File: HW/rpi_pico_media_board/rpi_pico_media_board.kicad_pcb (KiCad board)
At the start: 2 copper layers, 134 parts, among them IC100 LS1205EVD33, J200 Conn_01x04_Pin, J201 Conn_01x04_Pin, J300 AudioJack3_Ground_SwitchTR, J400 TF-01A, Q100 T2N7002AK, Q500 T2N7002AK, Q501 T2N7002AK, Q502 T2N7002AK, SW200 SW_DPDT_XLX, U100 HT7533-1, U200 RaspberryPi_Pico, U202 mems-mic, U203 mems-mic, U300 PCM5102A, U600 PCF8563TS, Y600 32768Hz

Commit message: DRC cleanup
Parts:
- removed C109, C110: 22uF, Capacitor_SMD:C_0603_1608Metric
- removed IC100: LS1205EVD33, rpi_pico_media_board_power:LS1205EVD33
- removed J100: ~, Connector_BarrelJack:BarrelJack_GCT_DCJ200-10-A_Horizontal
- removed R108: 10R, Resistor_SMD:R_0805_2012Metric
- removed R109: 510R, Resistor_SMD:R_0402_1005Metric
- removed R110: 12kR, Resistor_SMD:R_0402_1005Metric
- removed SW500, SW501, SW502, SW503, SW504, SW505, SW506, SW507, SW508, SW509, SW510, SW511: ~, rpi_pico_media_board:SW_PUSH_6mm_H5mm
- added J1: Barrel_Jack_Switch_Pin3Ring, Connector_BarrelJack:BarrelJack_GCT_DCJ200-10-A_Horizontal, F.Cu at (205.8, 18.3)
- added L101: 2u2H, Inductor_SMD:L_1008_2520Metric, F.Cu at (186.2, 125.8)
- added R306: 22R, Resistor_SMD:R_0603_1608Metric, F.Cu at (206.7, 36.2)
- added R307: 22R, Resistor_SMD:R_0603_1608Metric, F.Cu at (206.7, 38.8)
- added R308: 470R, Resistor_SMD:R_0805_2012Metric, F.Cu at (202.5, 36.5)
- added R309: 470R, Resistor_SMD:R_0805_2012Metric, F.Cu at (202.5, 39.4)
- added U500: SW, rpi_pico_media_board:SW_PUSH_6mm_H5mm, F.Cu at (189.7, 18.3)
- added U501: SW, rpi_pico_media_board:SW_PUSH_6mm_H5mm, F.Cu at (189.7, 26.8)
- added U502: SW, rpi_pico_media_board:SW_PUSH_6mm_H5mm, F.Cu at (189.7, 35.4)
- added U503: SW, rpi_pico_media_board:SW_PUSH_6mm_H5mm, F.Cu at (189.7, 43.9)
- added U504: SW, rpi_pico_media_board:SW_PUSH_6mm_H5mm, F.Cu at (222.9, 17.4)
- added U505: SW, rpi_pico_media_board:SW_PUSH_6mm_H5mm, F.Cu at (222.9, 25.9)
- added U506: SW, rpi_pico_media_board:SW_PUSH_6mm_H5mm, F.Cu at (222.9, 34.5)
- added U507: SW, rpi_pico_media_board:SW_PUSH_6mm_H5mm, F.Cu at (222.9, 43.0)
- added U508: SW, rpi_pico_media_board:SW_PUSH_6mm_H5mm, F.Cu at (222.9, 51.6)
- added U509: SW, rpi_pico_media_board:SW_PUSH_6mm_H5mm, F.Cu at (233.5, 17.4)
- added U510: SW, rpi_pico_media_board:SW_PUSH_6mm_H5mm, F.Cu at (233.5, 25.9)
- added U511: SW, rpi_pico_media_board:SW_PUSH_6mm_H5mm, F.Cu at (233.5, 34.5)
- C100: value 22uF -> 1uF; footprint Capacitor_SMD:C_1206_3216Metric -> Capacitor_SMD:C_0603_1608Metric
- C101: value 100nF -> 1uF; footprint Capacitor_SMD:C_0402_1005Metric -> Capacitor_SMD:C_0603_1608Metric
- C102: value 100nF -> 22uF; footprint Capacitor_SMD:C_0402_1005Metric -> Capacitor_SMD:C_1206_3216Metric
- C103: value 22uF -> 4u7F; footprint Capacitor_SMD:C_1206_3216Metric -> Capacitor_SMD:C_0603_1608Metric
- C104: value 22uF -> 22pF; footprint Capacitor_SMD:C_1206_3216Metric -> Capacitor_SMD:C_0603_1608Metric
- C105: value 4u7F -> 22uF; footprint Capacitor_SMD:C_0603_1608Metric -> Capacitor_SMD:C_1206_3216Metric
- C106: value 22pF -> 22uF; footprint Capacitor_SMD:C_0402_1005Metric -> Capacitor_SMD:C_1206_3216Metric
- L100: value 2u2H -> 10nH; footprint Inductor_SMD:L_1008_2520Metric -> Inductor_SMD:L_0603_1608Metric
- R100, R107: value 100kR -> 12kR; footprint Resistor_SMD:R_0402_1005Metric -> Resistor_SMD:R_0603_1608Metric
- R101: value 4k7R -> 12kR; footprint Resistor_SMD:R_0402_1005Metric -> Resistor_SMD:R_0603_1608Metric
- R102, R104: value 12kR -> 100kR; footprint Resistor_SMD:R_0402_1005Metric -> Resistor_SMD:R_0603_1608Metric
- R103: value 12kR -> 453kR; footprint Resistor_SMD:R_0402_1005Metric -> Resistor_SMD:R_0603_1608Metric
- R105: value 100kR -> 10R; footprint Resistor_SMD:R_0402_1005Metric -> Resistor_SMD:R_0805_2012Metric
- R106: value 453kR -> 510R; footprint Resistor_SMD:R_0402_1005Metric -> Resistor_SMD:R_0603_1608Metric
- R304, R305: value 470R -> 22R; footprint Resistor_SMD:R_0805_2012Metric -> Resistor_SMD:R_0603_1608Metric
- R507, R508, R509, R510, R511, R512: footprint Resistor_SMD:R_0402_1005Metric -> Resistor_SMD:R_0603_1608Metric
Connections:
- C101 pad 1: /[1]Power/PWR_EN -> +5V
- C102 pad 1: /[1]Power/EFUSE_SS -> +5V
- C103 pad 1: +5V -> PG_3V3
- C104 pad 1: +5V -> +3.3V
- C104 pad 2: GND -> /[1]Power/FB_3V3
- C105 pad 1: PG_3V3 -> +3.3V
- C106 pad 2: /[1]Power/FB_3V3 -> GND
- C107 pad 1: +3.3V -> /[1]Power/+5V_FILT
- C108 pad 1: +3.3V -> +3.3VA
- J400 pad 6: unconnected-(J400-VSS-Pad6) -> GND
- L100 pad 1: /[1]Power/SW_3V3 -> VCC
- L100 pad 2: +3.3V -> +5V
- R100 pad 1: VCC -> PG_3V3
- R100 pad 2: /[1]Power/PWR_EN -> +5V
- R101 pad 1: /[1]Power/EFUSE_ILIM -> +5V
- R101 pad 2: GND -> /[1]Power/EN_3V3
- R102 pad 1: /[1]Power/EFUSE_VCP -> PG_3V3
- R102 pad 2: VCC -> GND
- R103 pad 1: PG_3V3 -> +3.3V
- R103 pad 2: +5V -> /[1]Power/FB_3V3
- R104 pad 1: +5V -> /[1]Power/FB_3V3
- R104 pad 2: /[1]Power/EN_3V3 -> GND
- R105 pad 1: PG_3V3 -> /[1]Power/+5V_FILT
- R105 pad 2: GND -> +5V
- R106 pad 1: +3.3V -> /[1]Power/LED_PWR_A
- R106 pad 2: /[1]Power/FB_3V3 -> +5V
- R107 pad 1: /[1]Power/FB_3V3 -> Net-(Q100-G)
- R107 pad 2: GND -> PG_3V3
- R304 pad 1: /[3]PCM5102/OUTR -> GND
- R304 pad 2: /[3]PCM5102/OUT_R -> /[3]PCM5102/FLT
- R305 pad 1: /[3]PCM5102/OUTL -> GND
- R305 pad 2: /[3]PCM5102/OUT_L -> /[3]PCM5102/DEMP
- U300 pad 10: GND -> /[3]PCM5102/DEMP
- U300 pad 11: GND -> /[3]PCM5102/FLT
- U300 pad 16: GND -> /[3]PCM5102/FMT
- U300 pad 17: +3.3V -> /[3]PCM5102/XSMT
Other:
- copper layers 2 -> 4
- rule pad_to_mask_clearance: 0 -> 0.038

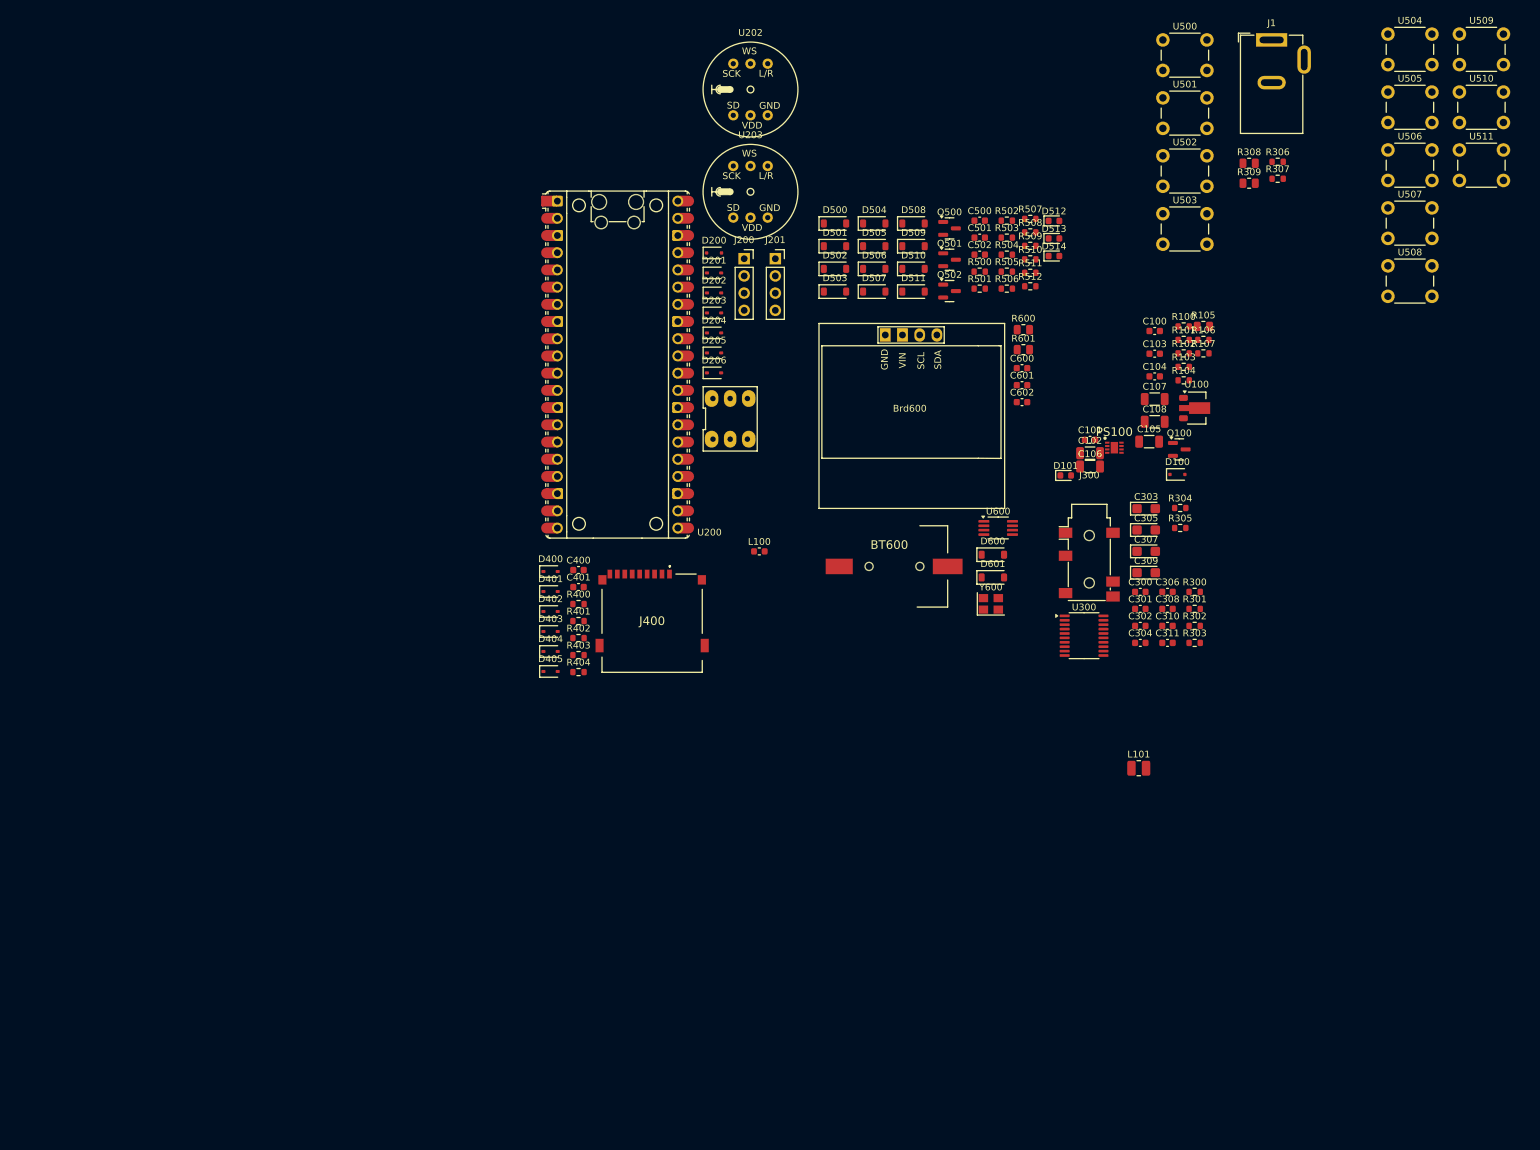
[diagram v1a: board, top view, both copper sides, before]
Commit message: PCB initial placement
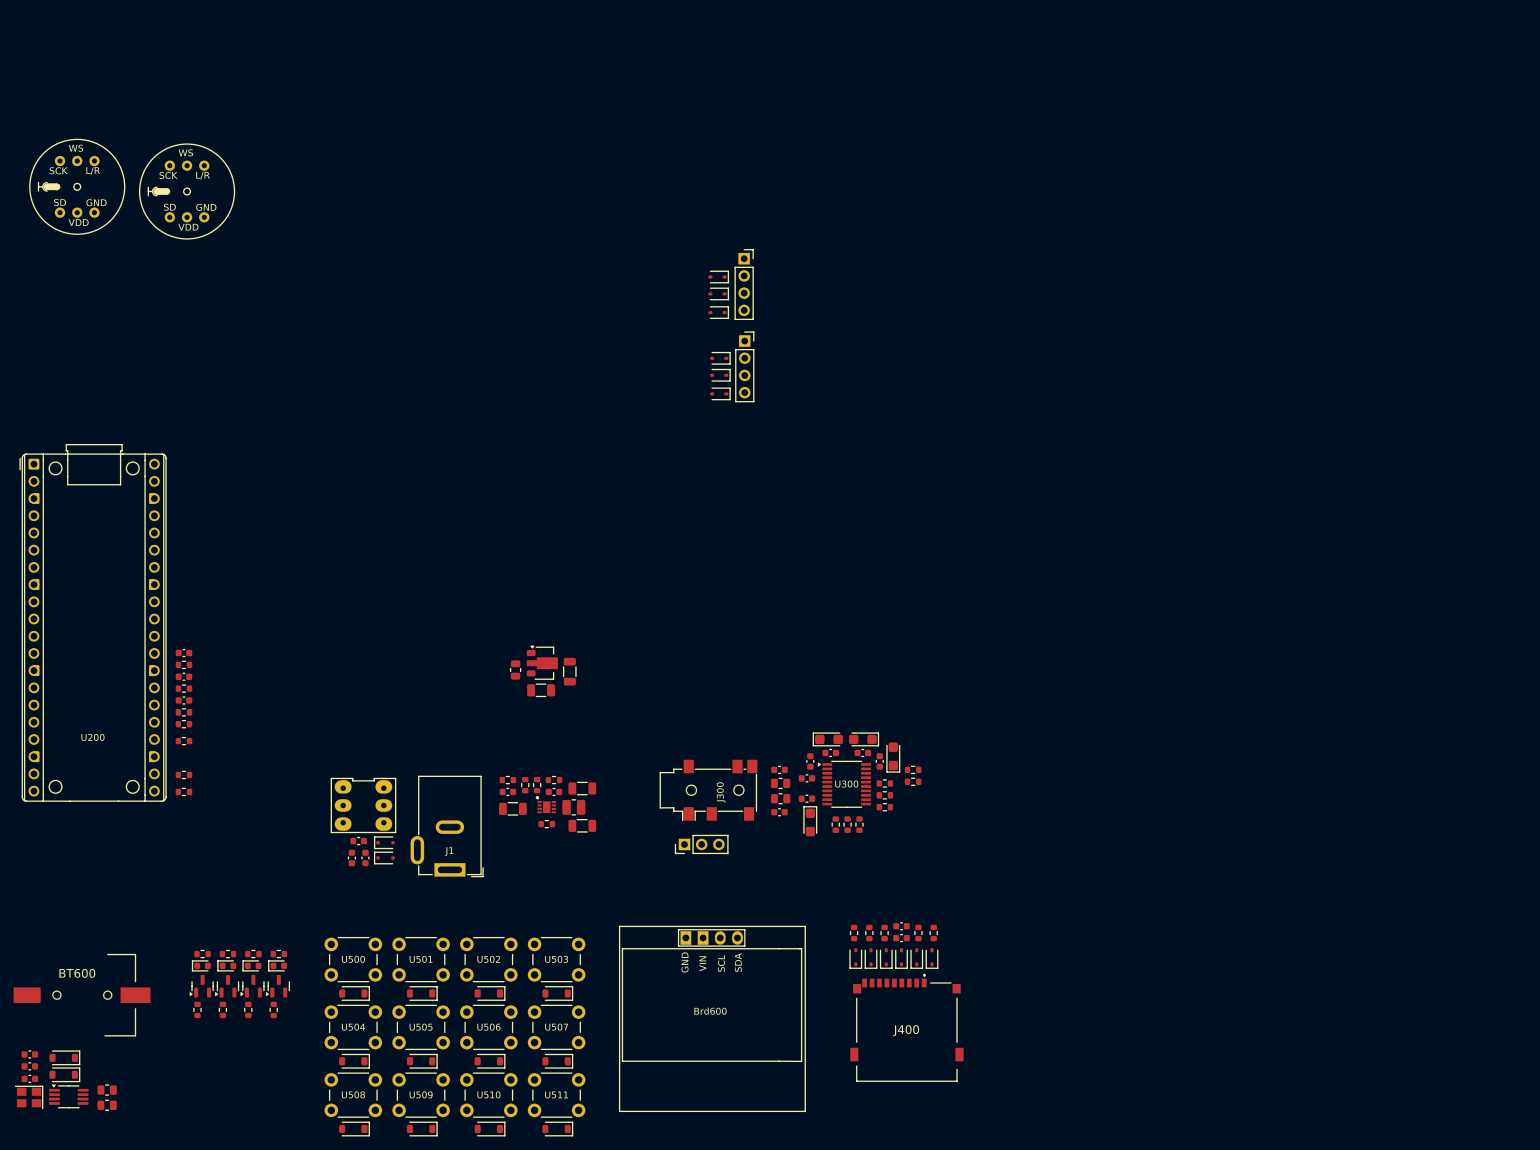
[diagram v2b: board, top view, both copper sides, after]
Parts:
- added J301: Conn_01x03_Pin, Connector_PinHeader_2.54mm:PinHeader_1x03_P2.54mm_Vertical, F.Cu at (119.1, 137.0)
- U200: footprint Module_RaspberryPi_Pico:RaspberryPi_Pico_Common -> Module_RaspberryPi_Pico:RaspberryPi_Pico_Common_THT
- moved U509 219.8 mm to (77.0, 171.8)
- moved U504 212.5 mm to (67.0, 161.8)
- moved U510 206.7 mm to (87.0, 171.8)
- moved U505 199.4 mm to (77.0, 161.8)
- moved U508 196.9 mm to (67.0, 171.8)
- moved U511 193.6 mm to (97.0, 171.8)
- moved U506 186.2 mm to (87.0, 161.8)
- moved U500 181.3 mm to (67.0, 151.8)
- moved C600 179.1 mm to (22.5, 169.8), turned to 180 degrees
- moved C602 177.3 mm to (22.5, 171.6), turned to 180 degrees
- moved R600 177.2 mm to (33.9, 175.5), turned to 180 degrees
- moved C601 176.7 mm to (22.5, 168.0), turned to 180 degrees
- moved R601 173.9 mm to (33.9, 173.2), turned to 180 degrees
- moved U507 173.1 mm to (97.0, 161.8)
- moved J1 172.4 mm to (84.5, 140.8), turned to 180 degrees
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
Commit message: Very initial PCB layout
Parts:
- removed D204: PESD3V3L1BA,115, Diode_SMD:D_SOD-323
- added C109: 22uF, Capacitor_SMD:C_1206_3216Metric, F.Cu at (174.8, 115.5)
- added C110: 22uF, Capacitor_SMD:C_1206_3216Metric, F.Cu at (178.8, 112.5)
- added R108: 12kR, Resistor_SMD:R_0603_1608Metric, F.Cu at (242.8, 89.0)
- added U101: HT7533-1, Package_TO_SOT_SMD:SOT-89-3, F.Cu at (178.5, 116.5)
- BT600: moved to B.Cu
- J201: value Conn_01x04_Pin -> Conn_01x03; footprint Connector_PinSocket_2.54mm:PinSocket_1x04_P2.54mm_Vertical -> Connector_PinSocket_2.54mm:PinSocket_1x03_P2.54mm_Vertical
- R106: value 510R -> 10R; footprint Resistor_SMD:R_0603_1608Metric -> Resistor_SMD:R_0805_2012Metric
- R107: value 12kR -> 510R
- moved C601 214.2 mm to (216.5, 77.3), turned to 0 degrees
- moved D600 213.3 mm to (221.5, 79.9), turned to 0 degrees
- moved C600 212.0 mm to (213.2, 77.2)
- moved D601 209.6 mm to (216.2, 79.9)
- moved C602 209.5 mm to (211.4, 81.0)
- moved U600 209.5 mm to (217.1, 83.7)
- moved Y600 209.5 mm to (211.3, 83.8)
- moved R600 209.3 mm to (222.4, 84.6)
- moved R601 209.3 mm to (222.4, 82.3)
- moved BT600 206.1 mm to (216.3, 71.0)
- moved D101 193.4 mm to (241.1, 89.0), turned to -90 degrees
- moved Q100 191.6 mm to (238.1, 89.0), turned to 0 degrees
- moved R107 190.9 mm to (235.1, 89.0)
- moved R511 188.7 mm to (232.9, 89.0), turned to 90 degrees
- moved D514 187.7 mm to (231.2, 88.9), turned to -90 degrees
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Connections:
- net /[1]Power/+5V_FILT renamed /[1]Power/+5V_FILT_1
- C108 pad 1: +3.3VA -> +3.3VA_PCM
- C304 pad 1: +3.3VA -> +3.3VA_PCM
- C305 pad 1: +3.3VA -> +3.3VA_PCM
- C306 pad 1: +3.3VA -> +3.3VA_PCM
- C307 pad 1: +3.3VA -> +3.3VA_PCM
- R106 pad 1: /[1]Power/LED_PWR_A -> /[1]Power/+5V_FILT_2
- R107 pad 1: Net-(Q100-G) -> /[1]Power/LED_PWR_A
- R107 pad 2: PG_3V3 -> +5V
- U100 pad 3: +3.3VA -> +3.3VA_PCM
- U202 pad 1: +3.3VA -> +3.3VA_INMP
- U202 pad 6: +3.3VA -> +3.3VA_INMP
- U203 pad 1: +3.3VA -> +3.3VA_INMP
- U300 pad 1: +3.3VA -> +3.3VA_PCM
- U300 pad 20: +3.3VA -> +3.3VA_PCM

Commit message: minor layout update
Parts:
- moved R106 124.8 mm to (60.0, 93.2)
- moved C109 124.8 mm to (52.0, 93.2)
- moved C110 124.8 mm to (56.0, 90.2)
- moved U101 124.8 mm to (55.8, 94.2)
- moved R306 122.1 mm to (54.5, 80.8), turned to 0 degrees
- moved R307 121.2 mm to (54.5, 82.5), turned to 0 degrees
- moved R302 116.1 mm to (57.0, 82.7), turned to 90 degrees
- moved R304 114.9 mm to (54.4, 79.0), turned to 0 degrees
- moved R301 114.5 mm to (58.8, 82.7), turned to 90 degrees
- moved R404 113.8 mm to (55.0, 101.7), turned to -90 degrees
- moved R303 113.2 mm to (54.4, 77.2), turned to 0 degrees
- moved R300 112.8 mm to (60.5, 82.7), turned to 90 degrees
- moved R305 111.5 mm to (54.4, 75.5), turned to 0 degrees
- moved R400 111.4 mm to (57.2, 101.5), turned to -90 degrees
- moved D405 110.6 mm to (55.2, 105.1), turned to 90 degrees
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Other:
- board outline added: 100 x 80 mm

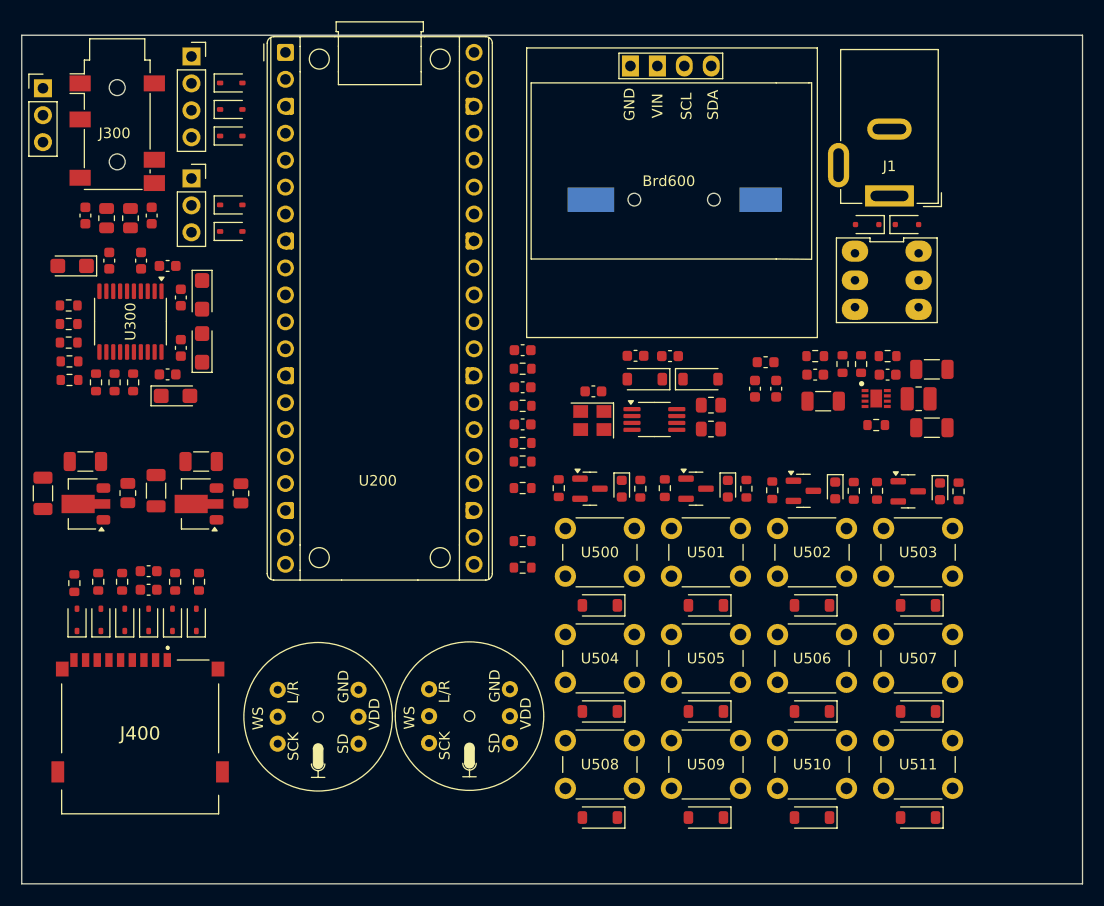
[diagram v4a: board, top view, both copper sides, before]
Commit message: PCB initial layout
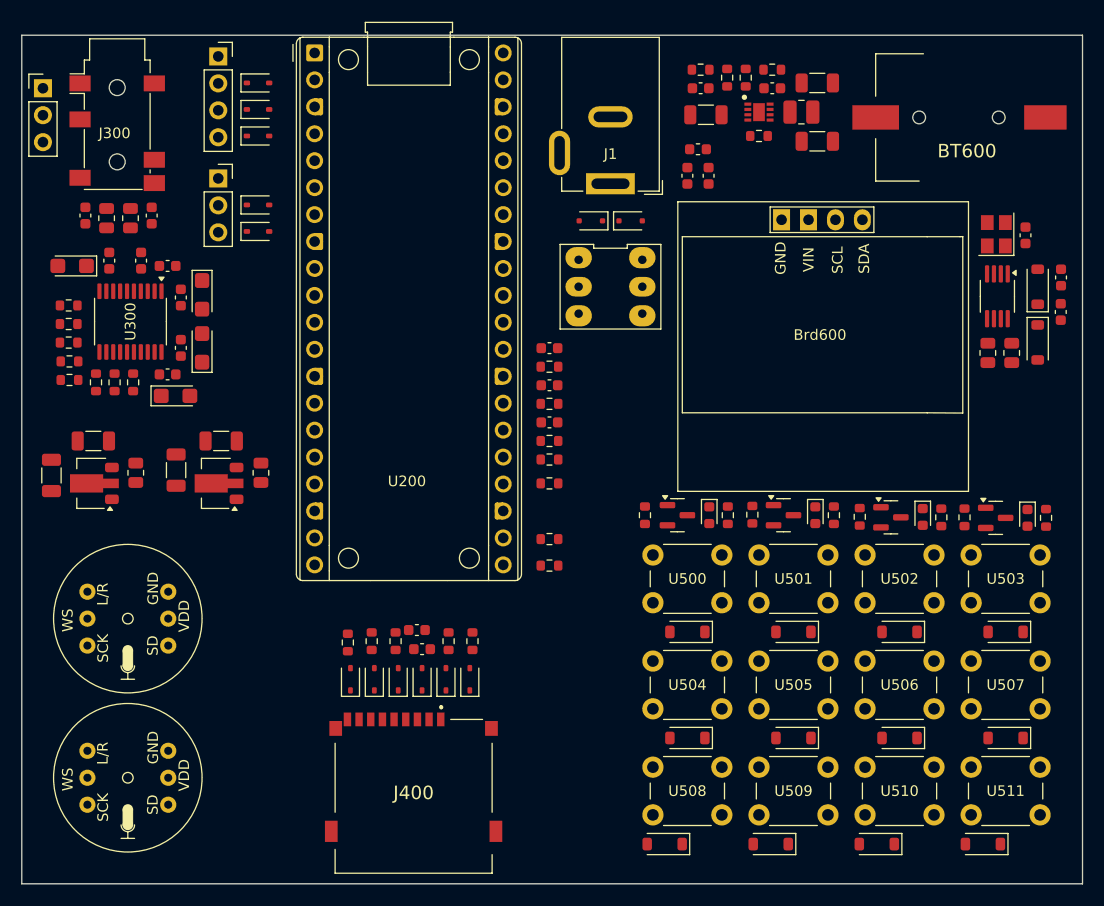
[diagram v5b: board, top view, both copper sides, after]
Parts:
- BT600: moved to F.Cu
- moved C602 43.3 mm to (144.6, 68.9), turned to 90 degrees
- moved Y600 41.9 mm to (141.9, 68.8), turned to 90 degrees
- moved C600 40.8 mm to (148.0, 72.8), turned to 90 degrees
- moved D601 38.0 mm to (145.8, 73.7), turned to 90 degrees
- moved C601 37.1 mm to (147.9, 76.1), turned to -90 degrees
- moved U600 34.4 mm to (142.0, 74.6), turned to -90 degrees
- moved U203 32.7 mm to (60.0, 120.0)
- moved D600 32.0 mm to (145.8, 79.0), turned to -90 degrees
- moved R101 29.4 mm to (119.5, 59.5)
- moved L101 29.2 mm to (123.5, 57.2)
- moved C102 29.2 mm to (114.5, 57.5)
- moved PS100 29.2 mm to (119.5, 57.2)
- moved C104 29.1 mm to (120.8, 55.0)
- moved R100 29.1 mm to (116.5, 54.0)
- moved R103 29.1 mm to (120.8, 53.2)
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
